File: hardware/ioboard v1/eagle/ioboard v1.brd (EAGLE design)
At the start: 160 x 100 mm, 30 parts, among them IC1 MCP23017SO, IC3 ACPL-244, IC4 ACPL-244, K1 61300611021, K2 613006143121

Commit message: First board layout
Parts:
- added C1, C2: (no value), rcl:C0805
- added K4: 691214110003, Wuerth_Elektronik_eiCan_14_Terminal_Blocks_WR-TBL_2_0:691214110003
- added R1: (no value), rcl:R0805
- added RN7: (no value), dp_devices:RN8P-4R-CRA06S
- added SJ1: (no value), jumper:SJ
- added SW1: 418127270903, Eagle_Wuerth_Elektronik_Switch_Power_Elements:418127270903
- moved LED13 144.2 mm to (78.7, 17.8), turned to 90 degrees
- moved LED16 143.5 mm to (78.7, 6.35), turned to 90 degrees
- moved LED14 138.5 mm to (78.7, 14.0), turned to 90 degrees
- moved LED15 132.8 mm to (78.7, 10.2), turned to 90 degrees
- moved LED10 129.7 mm to (66.0, 14.0), turned to 90 degrees
- moved LED9 128.9 mm to (66.0, 17.8), turned to 90 degrees
- moved RN6 126.2 mm to (55.9, 17.8), turned to 270 degrees
- moved LED11 124.1 mm to (66.0, 10.2), turned to 90 degrees
- moved LED12 118.7 mm to (66.0, 6.35), turned to 90 degrees
- moved IC2 114.1 mm to (64.8, 29.2)
- moved RN5 112.7 mm to (55.9, 8.89), turned to 270 degrees
- moved LED2 106.3 mm to (30.5, 14.0), turned to 90 degrees
- moved LED1 100.0 mm to (30.5, 17.8), turned to 90 degrees
- moved IC1 99.9 mm to (44.5, 15.2), turned to 90 degrees
- moved RN3 98.3 mm to (25.4, 20.3), turned to 180 degrees
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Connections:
- removed net N$19: K1.6, K2.1
- removed net N$20: K1.5, K2.2
- removed net N$21: K1.4, K2.3
- removed net N$22: K1.3, K2.4
- removed net N$23: K1.2, K2.5
- removed net N$24: K1.1, K2.6
- removed net VSS: IC1.10
- new net !RST: C2.1, IC1.18, RN7.4, SJ1.1
- new net ADDR0: IC1.15, RN7.3, SW1.6
- new net ADDR1: IC1.16, RN7.2, SW1.5
- new net ADDR2: IC1.17, RN7.1, SW1.4
- new net AGND: IC3.2, IC3.4, IC3.6, IC3.8, IC4.2, IC4.4, IC4.6, IC4.8, K4.3
- new net INT: IC1.20, K1.1, K2.1, R1.2
- new net RST_EXT: K1.6, K2.6, SJ1.2
- new net SCL: IC1.12, K1.2, K2.2
- new net SDA: IC1.13, K1.5, K2.5
- new net V+: IC2.10, K4.1
- net GND: now also C1.2, C2.2, IC1.10, K1.4, K2.4, K4.2, SW1.1, SW1.2, SW1.3; no longer IC3.2, IC3.4, IC3.6, IC3.8, IC4.2, IC4.4, IC4.6, IC4.8
- net IN6: no longer INPUT.9
- net IN7: now also INPUT.9
- net OUT0: now also IC2.11, OUTPUT.15; no longer IC2.18
- net OUT1: now also IC2.12; no longer IC2.17, OUTPUT.15
- net OUT2: now also IC2.13; no longer IC2.16
- net OUT3: now also IC2.14; no longer IC2.15
- net OUT4: now also IC2.15; no longer IC2.14
- net OUT5: now also IC2.16; no longer IC2.13
- net OUT6: now also IC2.17; no longer IC2.12
- net OUT7: now also IC2.18; no longer IC2.11
- net OUT_L0: now also IC2.5, RN5.4; no longer IC2.1, RN5.1
- net OUT_L1: now also IC2.6, RN5.3; no longer IC2.2, RN5.2
- net OUT_L2: now also IC2.7, RN5.2; no longer IC2.3, RN5.3
- net OUT_L3: now also IC2.8, RN5.1; no longer IC2.4, RN5.4
- net OUT_L4: now also IC2.1, RN6.4; no longer IC2.5, RN6.1
- net OUT_L5: now also IC2.2, RN6.3; no longer IC2.6, RN6.2
- net OUT_L6: now also IC2.3, RN6.2; no longer IC2.7, RN6.3
- net OUT_L7: now also IC2.4, RN6.1; no longer IC2.8, RN6.4
- net VDD: now also C1.1, K1.3, K2.3, R1.1, RN7.5, RN7.6, RN7.7, RN7.8
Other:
- board size 160 x 100 mm -> 88.9 x 51.7 mm

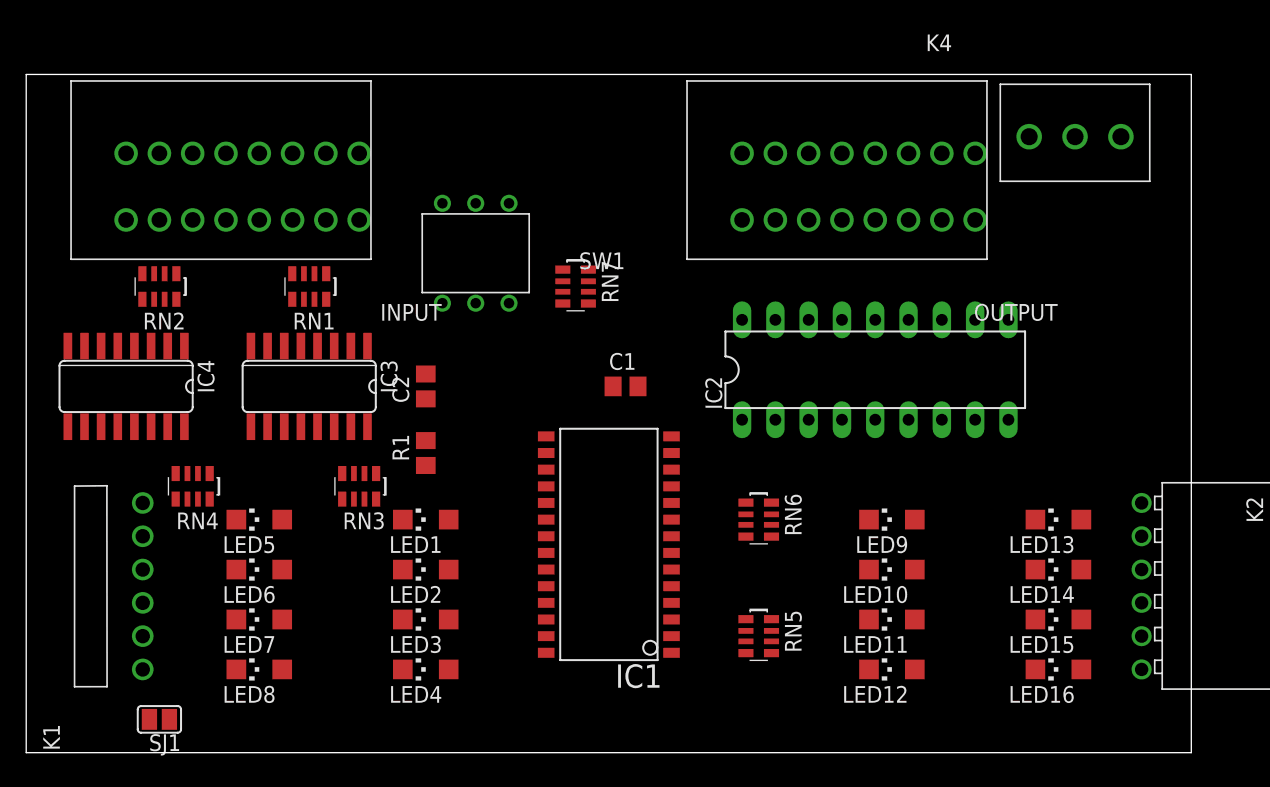
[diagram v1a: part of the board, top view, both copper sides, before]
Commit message: First routing attempt aith autorouter
But no rules, just to know the routing is possible
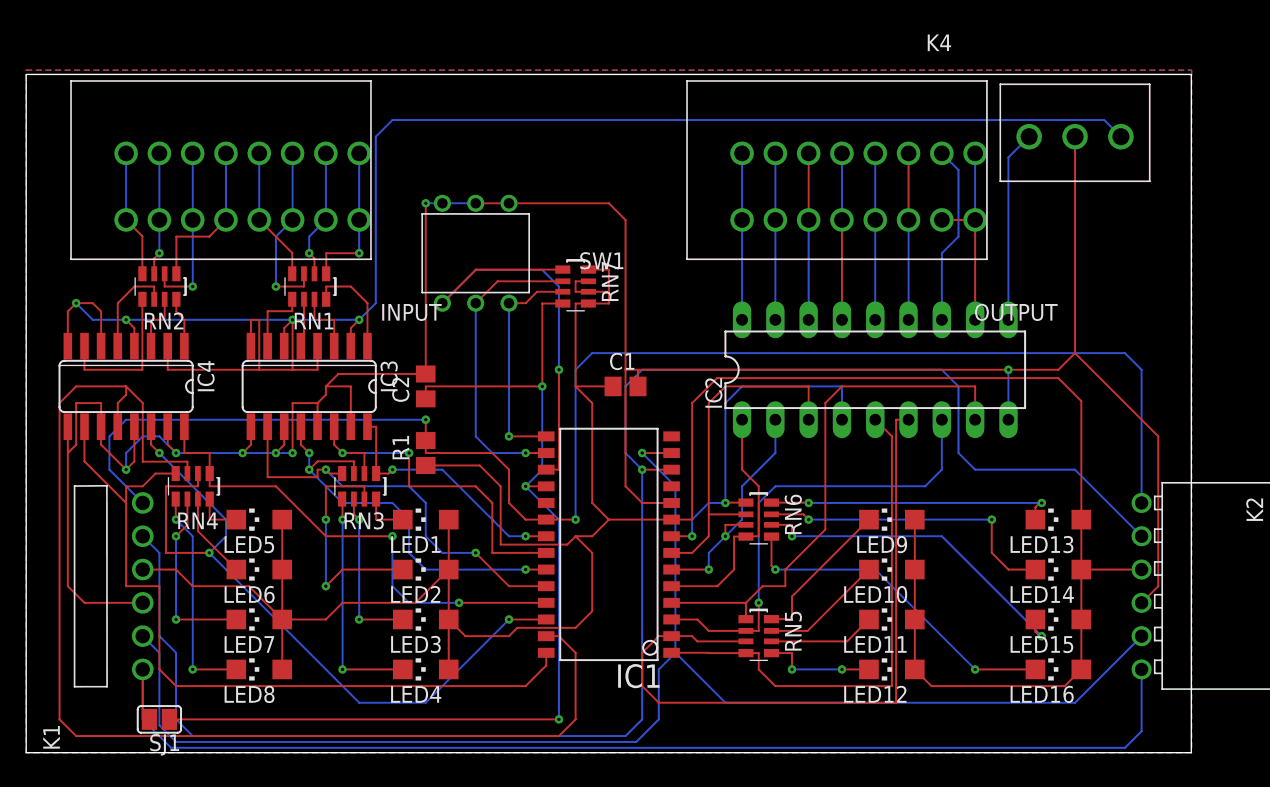
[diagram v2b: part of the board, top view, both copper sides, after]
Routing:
- net VDD: track 0.00 -> 215.8 mm
- net GND: track 0.00 -> 209.4 mm, vias 0 -> 7
- net AGND: track 0.00 -> 135.0 mm, vias 0 -> 4
- net SCL: track 0.00 -> 127.9 mm, vias 0 -> 1
- net INT: track 0.00 -> 114.2 mm, vias 0 -> 2
- net SDA: track 0.00 -> 110.0 mm, vias 0 -> 1
- net IN_L6: track 0.00 -> 91.9 mm
- net RST_EXT: track 0.00 -> 90.5 mm
- net !RST: track 0.00 -> 76.0 mm, vias 0 -> 3
- net IN_L7: track 0.00 -> 59.5 mm
- net IN_L5: track 0.00 -> 57.4 mm, vias 0 -> 3
- net OUT_L1: track 0.00 -> 53.6 mm
- net OUT_L3: track 0.00 -> 40.2 mm
- net OUT_L0: track 0.00 -> 39.4 mm
- net IN_L4: track 0.00 -> 38.1 mm, vias 0 -> 2
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- added copper zone on layer 1, net GND
- added copper zone on layer 16, net GND

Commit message: Ordernumbers completed
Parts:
- moved LED13 16.5 mm to (62.2, 17.8)
- moved LED14 16.5 mm to (62.2, 14.0)
- moved LED15 16.5 mm to (62.2, 10.2)
- moved LED16 16.5 mm to (62.2, 6.35)
- moved RN5 15.9 mm to (69.8, 16.5)
- moved LED10 8.89 mm to (74.9, 14.0)
- moved LED11 8.89 mm to (74.9, 10.2)
- moved LED12 8.89 mm to (74.9, 6.35)
- moved LED9 8.89 mm to (74.9, 17.8)
- moved RN3 3.81 mm to (25.4, 16.5), turned to 270 degrees
- moved RN4 3.81 mm to (12.7, 16.5), turned to 270 degrees
- moved SJ1 1.27 mm to (10.2, 3.81)
- moved RN6 1.27 mm to (55.9, 16.5)
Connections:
- net OUT0: no longer OUTPUT.15
- net OUT1: now also OUTPUT.15
- net OUT_L0: now also IC2.8; no longer IC2.5
- net OUT_L1: now also IC2.7; no longer IC2.6
- net OUT_L2: now also IC2.6; no longer IC2.7
- net OUT_L3: now also IC2.5; no longer IC2.8
- net OUT_L4: now also IC2.4; no longer IC2.1
- net OUT_L5: now also IC2.3; no longer IC2.2
- net OUT_L6: now also IC2.2; no longer IC2.3
- net OUT_L7: now also IC2.1; no longer IC2.4
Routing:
- net IN_L2: track 30.9 -> 106.3 mm, vias 3 -> 2
- net IN_L6: track 91.9 -> 151.7 mm, vias 0 -> 4
- net GND: track 209.4 -> 234.3 mm, vias 7 -> 8
- net IN_L1: track 27.9 -> 51.0 mm
- net N$26: track 9.37 -> 30.8 mm
- net N$31: track 22.2 -> 6.14 mm, vias 2 -> 0
- net N$32: track 23.4 -> 7.34 mm
- net INT: track 114.2 -> 99.5 mm, vias 2 -> 1
- net IN_L4: track 38.1 -> 52.3 mm, vias 2 -> 3
- net N$33: track 26.2 -> 12.0 mm, vias 2 -> 0
- net N$34: track 25.6 -> 11.7 mm, vias 2 -> 0
- net N$18: track 17.9 -> 4.55 mm, vias 2 -> 0
- net AGND: track 135.0 -> 121.9 mm, vias 4 -> 6
- net N$12: track 5.45 -> 18.4 mm
- net SDA: track 110.0 -> 101.7 mm
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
